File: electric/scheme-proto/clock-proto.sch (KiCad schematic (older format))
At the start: 135 parts

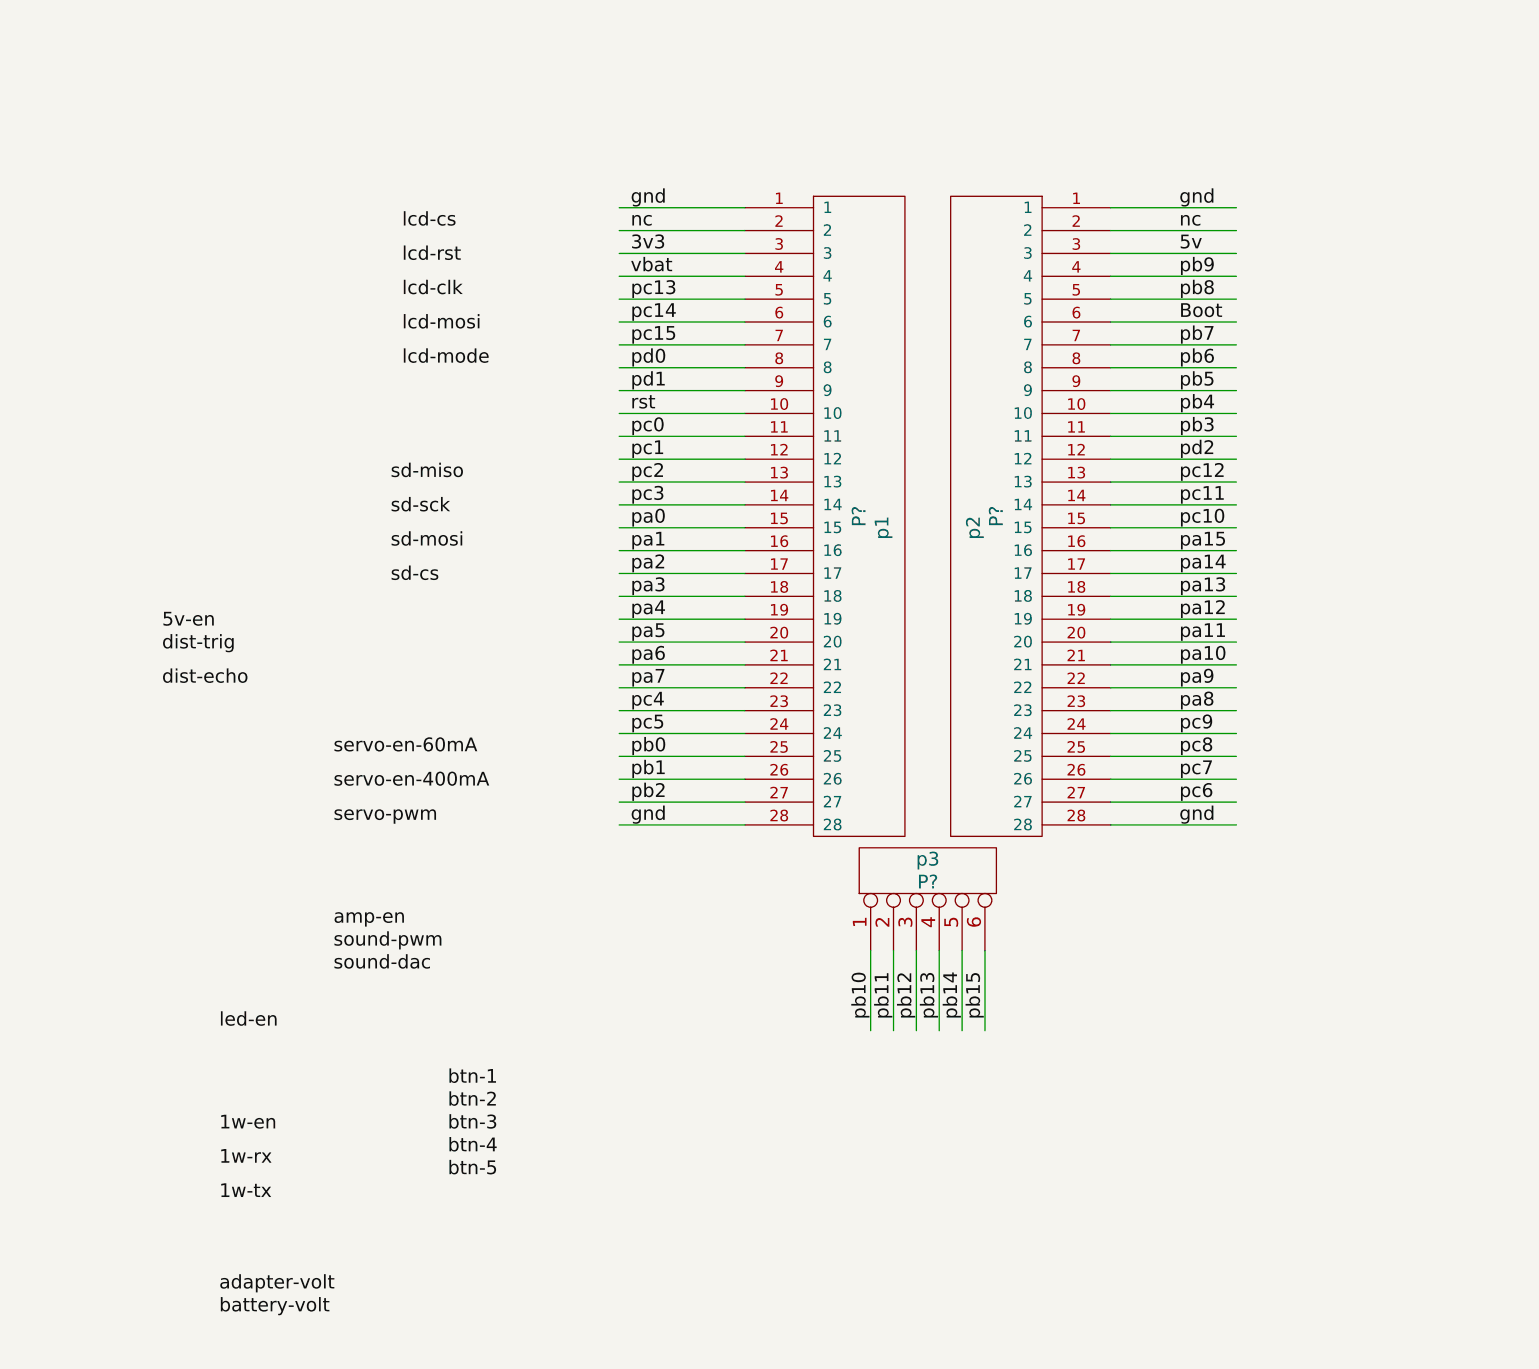
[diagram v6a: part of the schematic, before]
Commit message: Connecte wires to sockets.
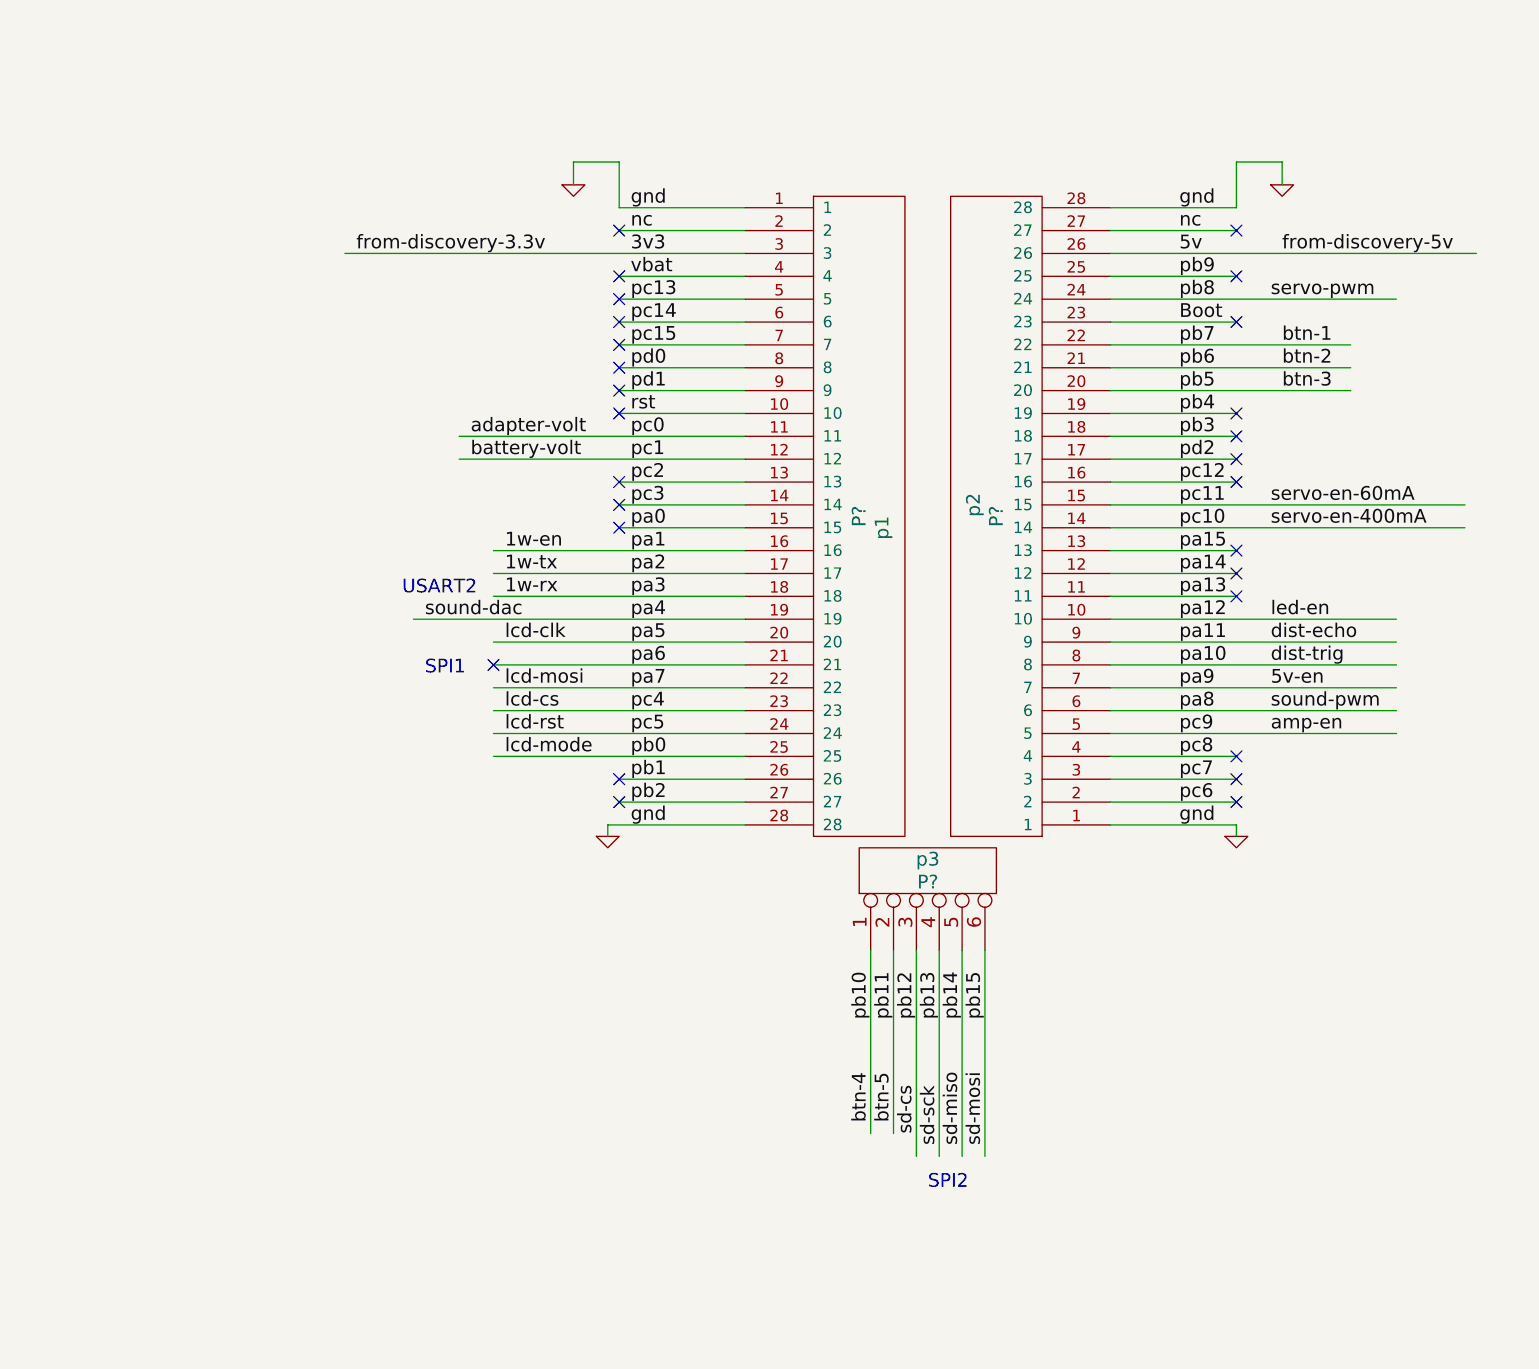
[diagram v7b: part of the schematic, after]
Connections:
- wire segments 422 -> 430
- no-connect marks 6 -> 33
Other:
- note added: "SPI1"
- note added: "SPI2"
- note added: "USART2"
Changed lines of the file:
@@
 F 3 "~" H 30400 18800 60  0000 C CNN
 	1    30200 18850
-	-1   0    0    -1
+	-1   0    0    1
 $EndComp
 $Comp
@@
 $EndComp
 Wire Wire Line
-	29650 20750 29650 21100
+	29650 20750 29650 21550
 Text Label 29650 21050 1    60   ~ 0
 pb10
@@
 pb15
 Wire Wire Line
-	29750 20750 29750 21100
-Wire Wire Line
-	29850 20750 29850 21100
-Wire Wire Line
-	29950 20750 29950 21100
-Wire Wire Line
-	30050 20750 30050 21100
-Wire Wire Line
-	30150 20750 30150 21100
+	29750 20750 29750 21550
+Wire Wire Line
+	29850 20750 29850 21650
+Wire Wire Line
+	29950 20750 29950 21650
+Wire Wire Line
+	30050 20750 30050 21650
+Wire Wire Line
+	30150 20750 30150 21650
 Wire Wire Line
 	29100 17500 28550 17500
@@
 	29100 17600 28550 17600
 Wire Wire Line
-	29100 17700 28550 17700
+	27350 17700 29100 17700
 Wire Wire Line
 	29100 17800 28550 17800
@@
 	29100 18400 28550 18400
 Wire Wire Line
-	29100 18500 28550 18500
-Wire Wire Line
-	29100 18600 28550 18600
+	27850 18500 29100 18500
+Wire Wire Line
+	27850 18600 29100 18600
 Wire Wire Line
 	29100 18700 28550 18700
@@
 	29100 18900 28550 18900
 Wire Wire Line
-	29100 19000 28550 19000
-Wire Wire Line
-	29100 19100 28550 19100
-Wire Wire Line
-	29100 19200 28550 19200
-Wire Wire Line
-	29100 19300 28550 19300
-Wire Wire Line
-	29100 19400 28550 19400
-Wire Wire Line
-	29100 19500 28550 19500
+	28000 19000 29100 19000
+Wire Wire Line
+	28000 19100 29100 19100
+Wire Wire Line
+	28000 19200 29100 19200
+Wire Wire Line
+	27650 19300 29100 19300
+Wire Wire Line
+	28000 19400 29100 19400
+Wire Wire Line
+	28000 19500 29100 19500
 $Comp
 L PNP Q?
@@
 Because servo-vcc could \nbe less then 3.3v if batteries \npack is very discharged.
 Wire Wire Line
-	29100 19600 28550 19600
-Wire Wire Line
-	29100 19700 28550 19700
-Wire Wire Line
-	29100 19800 28550 19800
-Wire Wire Line
-	29100 19900 28550 19900
+	28000 19600 29100 19600
+Wire Wire Line
+	28000 19700 29100 19700
+Wire Wire Line
+	28000 19800 29100 19800
+Wire Wire Line
+	28000 19900 29100 19900
 Wire Wire Line
 	29100 20000 28550 20000
@@
 	29100 20100 28550 20100
 Wire Wire Line
-	29100 20200 28550 20200
+	28500 20200 29100 20200
 Wire Wire Line
 	31250 17500 30700 17500
@@
 	31250 17600 30700 17600
 Wire Wire Line
-	31250 17700 30700 17700
+	30700 17700 32300 17700
 Wire Wire Line
 	31250 17800 30700 17800
 Wire Wire Line
-	31250 17900 30700 17900
+	30700 17900 31950 17900
 Wire Wire Line
 	31250 18000 30700 18000
 Wire Wire Line
-	31250 18100 30700 18100
-Wire Wire Line
-	31250 18200 30700 18200
-Wire Wire Line
-	31250 18300 30700 18300
+	30700 18100 31750 18100
+Wire Wire Line
+	30700 18200 31750 18200
+Wire Wire Line
+	30700 18300 31750 18300
 Wire Wire Line
 	31250 18400 30700 18400
@@
 	31250 18700 30700 18700
 Wire Wire Line
-	31250 18800 30700 18800
-Wire Wire Line
-	31250 18900 30700 18900
+	30700 18800 32250 18800
+Wire Wire Line
+	30700 18900 32250 18900
 Wire Wire Line
 	31250 19000 30700 19000
@@
 	31250 19200 30700 19200
 Wire Wire Line
-	31250 19300 30700 19300
-Wire Wire Line
-	31250 19400 30700 19400
-Wire Wire Line
-	31250 19500 30700 19500
-Wire Wire Line
-	31250 19600 30700 19600
-Wire Wire Line
-	31250 19700 30700 19700
-Wire Wire Line
-	31250 19800 30700 19800
+	30700 19300 31950 19300
+Wire Wire Line
+	30700 19400 31950 19400
+Wire Wire Line
+	30700 19500 31950 19500
+Wire Wire Line
+	30700 19600 31950 19600
+Wire Wire Line
+	30700 19700 31950 19700
+Wire Wire Line
+	30700 19800 31950 19800
 Wire Wire Line
 	31250 19900 30700 19900
@@
 Wire Wire Line
 	13800 17050 13800 17350
-Text Label 27600 17600 0    60   ~ 0
+Text Label 28050 19700 0    60   ~ 0
 lcd-cs
-Text Label 27600 17750 0    60   ~ 0
+Text Label 28050 19800 0    60   ~ 0
 lcd-rst
-Text Label 27600 17900 0    60   ~ 0
+Text Label 28050 19400 0    60   ~ 0
 lcd-clk
-Text Label 27600 18050 0    60   ~ 0
+Text Label 28050 19600 0    60   ~ 0
 lcd-mosi
-Text Label 27600 18200 0    60   ~ 0
+Text Label 28050 19900 0    60   ~ 0
 lcd-mode
-Text Label 27550 18700 0    60   ~ 0
+Text Label 30050 21600 1    60   ~ 0
 sd-miso
-Text Label 27550 18850 0    60   ~ 0
+Text Label 29950 21600 1    60   ~ 0
 sd-sck
-Text Label 27550 19000 0    60   ~ 0
+Text Label 30150 21600 1    60   ~ 0
 sd-mosi
-Text Label 27550 19150 0    60   ~ 0
+Text Label 29850 21550 1    60   ~ 0
 sd-cs
-Text Label 26550 19350 0    60   ~ 0
+Text Label 31400 19600 0    60   ~ 0
 5v-en
-Text Label 27300 19900 0    60   ~ 0
+Text Label 31400 18800 0    60   ~ 0
 servo-en-60mA
-Text Label 27300 20050 0    60   ~ 0
+Text Label 31400 18900 0    60   ~ 0
 servo-en-400mA
-Text Label 27300 20200 0    60   ~ 0
+Text Label 31400 17900 0    60   ~ 0
 servo-pwm
-Text Label 27300 20650 0    60   ~ 0
+Text Label 31400 19800 0    60   ~ 0
 amp-en
-Text Label 27300 20750 0    60   ~ 0
+Text Label 31400 19700 0    60   ~ 0
 sound-pwm
-Text Label 27300 20850 0    60   ~ 0
+Text Label 27700 19300 0    60   ~ 0
 sound-dac
-Text Label 26550 19450 0    60   ~ 0
+Text Label 31400 19500 0    60   ~ 0
 dist-trig
-Text Label 26550 19600 0    60   ~ 0
+Text Label 31400 19400 0    60   ~ 0
 dist-echo
-Text Label 26800 21100 0    60   ~ 0
+Text Label 31400 19300 0    60   ~ 0
 led-en
-Text Label 26800 21550 0    60   ~ 0
+Text Label 28050 19000 0    60   ~ 0
 1w-en
-Text Label 26800 21700 0    60   ~ 0
+Text Label 28050 19200 0    60   ~ 0
 1w-rx
-Text Label 26800 21850 0    60   ~ 0
+Text Label 28050 19100 0    60   ~ 0
 1w-tx
-Text Label 26800 22250 0    60   ~ 0
+Text Label 27900 18500 0    60   ~ 0
 adapter-volt
-Text Label 26800 22350 0    60   ~ 0
+Text Label 27900 18600 0    60   ~ 0
 battery-volt
-Text Label 27800 21350 0    60   ~ 0
+Text Label 31450 18100 0    60   ~ 0
 btn-1
-Text Label 27800 21450 0    60   ~ 0
+Text Label 31450 18200 0    60   ~ 0
 btn-2
-Text Label 27800 21550 0    60   ~ 0
+Text Label 31450 18300 0    60   ~ 0
 btn-3
-Text Label 27800 21650 0    60   ~ 0
+Text Label 29650 21500 1    60   ~ 0
 btn-4
-Text Label 27800 21750 0    60   ~ 0
+Text Label 29750 21500 1    60   ~ 0
 btn-5
+Text Label 27400 17700 0    60   ~ 0
+from-discovery-3.3v
+Text Label 31450 17700 0    60   ~ 0
+from-discovery-5v
+Wire Wire Line
+	31250 17500 31250 17300
+Wire Wire Line
+	31250 17300 31450 17300
+Wire Wire Line
+	31450 17300 31450 17400
+$Comp
+L GND #PWR?
+U 1 1 53042B2C
+P 31450 17400
+F 0 "#PWR?" H 31450 17400 30  0001 C CNN
+F 1 "GND" H 31450 17330 30  0001 C CNN
+F 2 "" H 31450 17400 60  0001 C CNN
+F 3 "" H 31450 17400 60  0001 C CNN
+	1    31450 17400
+	1    0    0    -1
+$EndComp
+NoConn ~ 28550 17600
+NoConn ~ 31250 17600
+Text Notes 27600 19200 0    60   ~ 0
+USART2
+Text Notes 27700 19550 0    60   ~ 0
+SPI1
+Text Notes 29900 21800 0    60   ~ 0
+SPI2
+NoConn ~ 28000 19500
+Wire Wire Line
+	28500 20200 28500 20250
+$Comp
+L GND #PWR?
+U 1 1 53048320
+P 28500 20250
+F 0 "#PWR?" H 28500 20250 30  0001 C CNN
+F 1 "GND" H 28500 20180 30  0001 C CNN
+F 2 "" H 28500 20250 60  0001 C CNN
+F 3 "" H 28500 20250 60  0001 C CNN
+	1    28500 20250
+	1    0    0    -1
+$EndComp
+Wire Wire Line
+	31250 20200 31250 20250
+$Comp
+L GND #PWR?
+U 1 1 53048327
+P 31250 20250
+F 0 "#PWR?" H 31250 20250 30  0001 C CNN
+F 1 "GND" H 31250 20180 30  0001 C CNN
+F 2 "" H 31250 20250 60  0001 C CNN
+F 3 "" H 31250 20250 60  0001 C CNN
+	1    31250 20250
+	1    0    0    -1
+$EndComp
+Wire Wire Line
+	28550 17500 28550 17300
+Wire Wire Line
+	28550 17300 28350 17300
+Wire Wire Line
+	28350 17300 28350 17400
+$Comp
+L GND #PWR?
+U 1 1 5304849A
+P 28350 17400
+F 0 "#PWR?" H 28350 17400 30  0001 C CNN
+F 1 "GND" H 28350 17330 30  0001 C CNN
+F 2 "" H 28350 17400 60  0001 C CNN
+F 3 "" H 28350 17400 60  0001 C CNN
+	1    28350 17400
+	1    0    0    -1
+$EndComp
+NoConn ~ 28550 18400
+NoConn ~ 28550 18300
+NoConn ~ 28550 18200
+NoConn ~ 28550 18100
+NoConn ~ 28550 18000
+NoConn ~ 28550 17900
+NoConn ~ 28550 17800
+NoConn ~ 28550 18700
+NoConn ~ 28550 18800
+NoConn ~ 28550 18900
+NoConn ~ 28550 20000
+NoConn ~ 28550 20100
+NoConn ~ 31250 20100
+NoConn ~ 31250 20000
+NoConn ~ 31250 19900
+NoConn ~ 31250 19200
+NoConn ~ 31250 19100
+NoConn ~ 31250 19000
+NoConn ~ 31250 18700
+NoConn ~ 31250 18600
+NoConn ~ 31250 18500
+NoConn ~ 31250 18400
+NoConn ~ 31250 18000
+NoConn ~ 31250 17800
 $EndSCHEMATC

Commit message: 3310 LCD should be fixed. All pins are of power_in type.
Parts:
- gave numbers to parts that had none: 134
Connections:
- wire segments 430 -> 431
